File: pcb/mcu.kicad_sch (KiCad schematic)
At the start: 33 parts, among them J1 Conn_01x02_Pin, SW1 SW_SPDT, SW2 SW_Push, SW3 SW_SPDT, U1 TLV1117LV33DCYR, U2 W25Q64JVSSIQ_C179171, U3 STM32H750VBTx, Y1 25 MHz

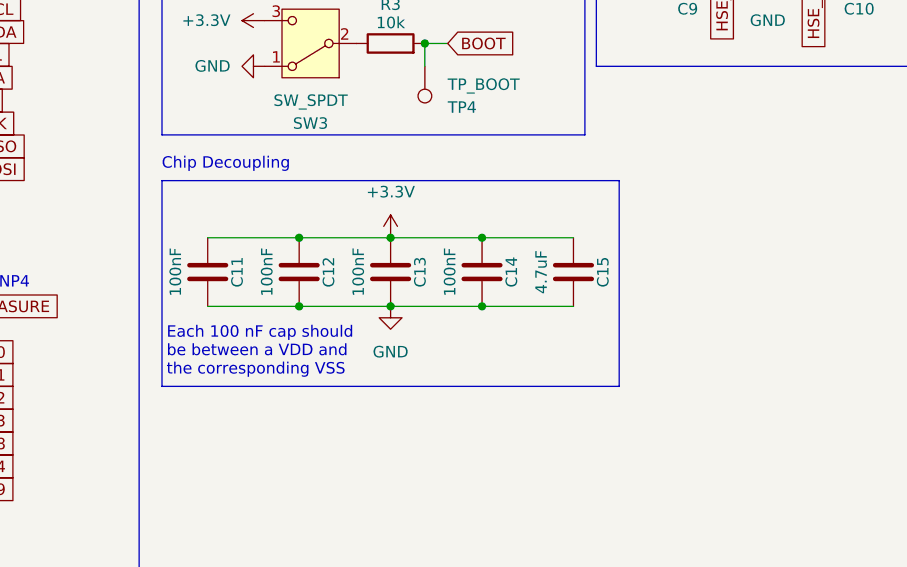
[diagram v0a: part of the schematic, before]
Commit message: [pcb] initial layout and power routing
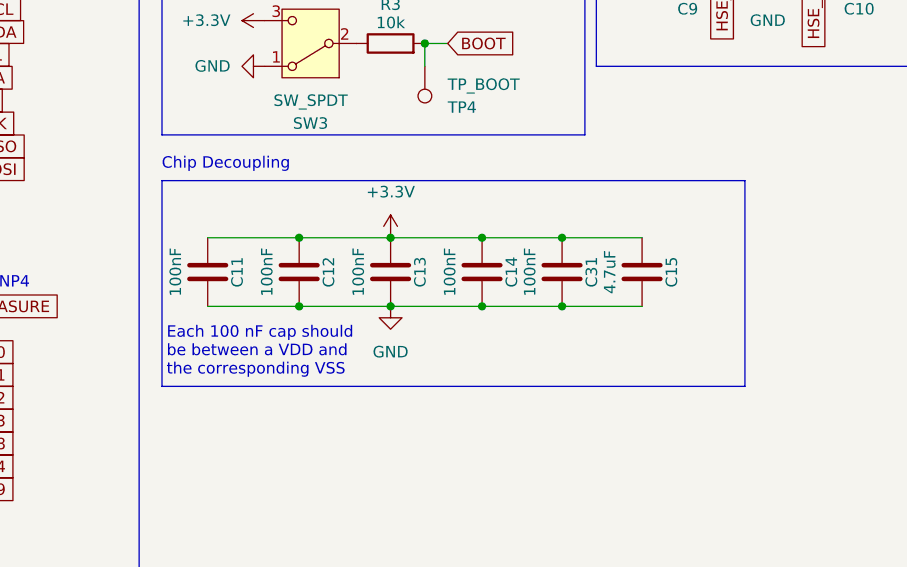
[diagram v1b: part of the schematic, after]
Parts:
- added C31: 100nF, Capacitor_SMD:C_0805_2012Metric_Pad1.18x1.45mm_HandSolder, symbol Device:C
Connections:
- net +3.3V: now also C31.1
- net GND: now also C31.2
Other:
- moved on the sheet: C15
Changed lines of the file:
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@@
 	(rectangle
 		(start 114.3 128.27)
-		(end 165.1 151.13)
+		(end 179.07 151.13)
 		(stroke
 			(width 0)
@@
 	)
 	(junction
+		(at 158.75 134.62)
+		(diameter 0)
+		(color 0 0 0 0)
+	)
+	(junction
 		(at 66.04 180.34)
 		(diameter 0)
@@
 	)
 	(junction
+		(at 158.75 142.24)
+		(diameter 0)
+		(color 0 0 0 0)
+	)
+	(junction
 		(at 62.23 35.56)
 		(diameter 0)
@@
 	(wire
 		(pts
+			(xy 158.75 142.24) (xy 167.64 142.24)
+		)
+		(stroke
+			(width 0)
+			(type default)
+		)
+	)
+	(wire
+		(pts
 			(xy 72.39 30.48) (xy 72.39 35.56)
 		)
@@
 	(wire
 		(pts
+			(xy 158.75 134.62) (xy 167.64 134.62)
+		)
+		(stroke
+			(width 0)
+			(type default)
+		)
+	)
+	(wire
+		(pts
 			(xy 72.39 20.32) (xy 72.39 30.48)
 		)
@@
 	(wire
 		(pts
-			(xy 90.17 39.37) (xy 91.44 39.37)
+			(xy 149.86 134.62) (xy 158.75 134.62)
 		)
 		(stroke
@@
 	(wire
 		(pts
-			(xy 149.86 134.62) (xy 160.02 134.62)
+			(xy 90.17 39.37) (xy 91.44 39.37)
 		)
 		(stroke
@@
 	(wire
 		(pts
-			(xy 149.86 142.24) (xy 160.02 142.24)
+			(xy 149.86 142.24) (xy 158.75 142.24)
 		)
 		(stroke
@@
 	(symbol
 		(lib_id "Device:C")
+		(at 158.75 138.43 0)
+		(unit 1)
+		(exclude_from_sim no)
+		(in_bom yes)
+		(on_board yes)
+		(dnp no)
+		(fields_autoplaced yes)
+		(property "Reference" "C31"
+			(at 162.052 138.43 90)
+			(effects
+				(font
+					(size 1.27 1.27)
+				)
+			)
+		)
+		(property "Value" "100nF"
+			(at 155.194 138.43 90)
+			(effects
+				(font
+					(size 1.27 1.27)
+				)
+			)
+		)
+		(property "Footprint" "Capacitor_SMD:C_0805_2012Metric_Pad1.18x1.45mm_HandSolder"
+			(at 159.7152 142.24 0)
+			(effects
+				(font
+					(size 1.27 1.27)
+				)
+				(hide yes)
+			)
+		)
+		(property "Datasheet" "~"
+			(at 158.75 138.43 0)
+			(effects
+				(font
+					(size 1.27 1.27)
+				)
+				(hide yes)
+			)
+		)
+		(property "Description" "Unpolarized capacitor"
+			(at 158.75 138.43 0)
+			(effects
+				(font
+					(size 1.27 1.27)
+				)
+				(hide yes)
+			)
+		)
+		(pin "1"
+		)
+		(pin "2"
+		)
+		(instances
+			(project "astra"
+				(path "/c0be3de2-9de4-4447-aa6f-537ea5f31aac/0c8c942c-f992-4664-b7a3-b87cb51e1584"
+					(reference "C31")
+					(unit 1)
+				)
+			)
+		)
+	)
+	(symbol
+		(lib_id "Device:C")
 		(at 191.77 101.6 90)
 		(mirror x)
@@
 	(symbol
 		(lib_id "Device:C")
-		(at 160.02 138.43 0)
+		(at 167.64 138.43 0)
 		(unit 1)
 		(exclude_from_sim no)
@@
 		(dnp no)
 		(property "Reference" "C15"
-			(at 163.322 138.43 90)
+			(at 170.942 138.43 90)
 			(effects
 				(font
@@
 		)
 		(property "Value" "4.7uF"
-			(at 156.464 138.43 90)
+			(at 164.084 138.43 90)
 			(effects
 				(font
@@
 		)
 		(property "Footprint" "Capacitor_SMD:C_0805_2012Metric_Pad1.18x1.45mm_HandSolder"
-			(at 160.9852 142.24 0)
+			(at 168.6052 142.24 0)
 			(effects
 				(font
@@
 		)
 		(property "Datasheet" "~"
-			(at 160.02 138.43 0)
+			(at 167.64 138.43 0)
 			(effects
 				(font
@@
 		)
 		(property "Description" "Unpolarized capacitor"
-			(at 160.02 138.43 0)
+			(at 167.64 138.43 0)
 			(effects
 				(font

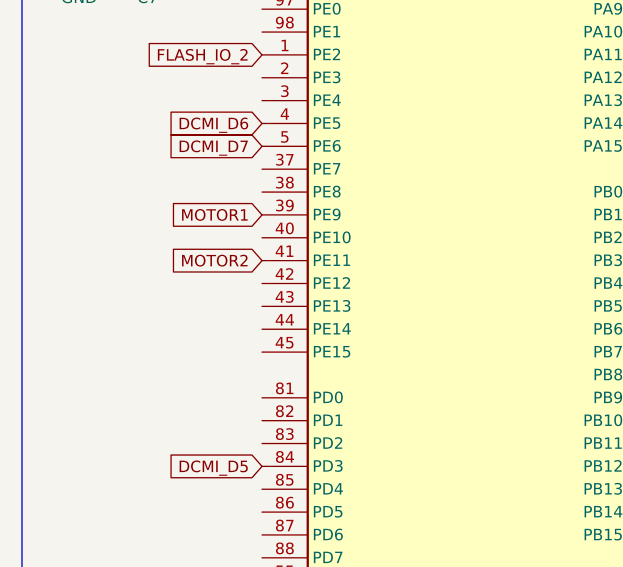
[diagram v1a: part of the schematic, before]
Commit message: [pcb] and [bom] add micro secure digital card interface socket connector
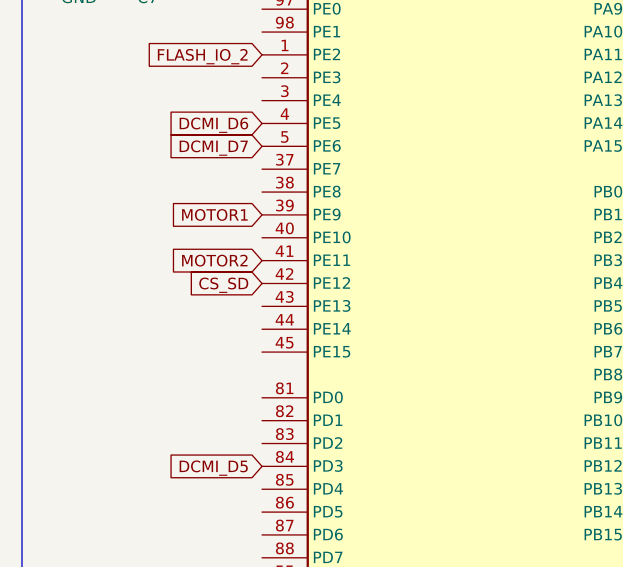
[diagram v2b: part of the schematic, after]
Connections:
- net CS_SD: now reaches U3.42 (PE12)
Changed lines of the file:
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@@
 			(font
 				(size 1.27 1.27)
-				(color 255 255 255 1)
 			)
 		)
@@
 			(font
 				(size 1.27 1.27)
-				(color 255 255 255 1)
 			)
 		)
@@
 			(font
 				(size 1.27 1.27)
-				(color 255 255 255 1)
 			)
 		)
@@
 			(font
 				(size 1.27 1.27)
-				(color 255 255 255 1)
 			)
 			(justify left)
@@
 			(font
 				(size 1.27 1.27)
-				(color 255 255 255 1)
 			)
 		)
@@
 			(effects
 				(font
+					(size 1.27 1.27)
+				)
+				(justify right)
+				(hide yes)
+			)
+		)
+	)
+	(global_label "CS_SD"
+		(shape input)
+		(at 41.91 99.06 180)
+		(fields_autoplaced yes)
+		(effects
+			(font
+				(size 1.27 1.27)
+			)
+			(justify right)
+		)
+		(property "Intersheetrefs" "${INTERSHEET_REFS}"
+			(at 32.9982 99.06 0)
+			(effects
+				(font

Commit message: [pcb] more routing
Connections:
- net DCMI_D0: now also U3.68 (PA9); no longer U3.63 (PC6)
- net DCMI_D2: now also U3.97 (PE0); no longer U3.65 (PC8)
- net DCMI_D3: now also U3.98 (PE1); no longer U3.66 (PC9)
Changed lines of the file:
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@@
+		)
+	)
+	(global_label "DCMI_D0"
+		(shape input)
+		(at 87.63 68.58 0)
+		(fields_autoplaced yes)
+		(effects
+			(font
+				(size 1.27 1.27)
+			)
+			(justify left)
+		)
+		(property "Intersheetrefs" "${INTERSHEET_REFS}"
+			(at 98.6585 68.58 0)
+			(effects
+				(font
+					(size 1.27 1.27)
+				)
+				(justify left)
+				(hide yes)
+			)
 		)
 	)
@@
 		)
 	)
+	(global_label "DCMI_PCLK"
+		(shape input)
+		(at 87.63 60.96 0)
+		(fields_autoplaced yes)
+		(effects
+			(font
+				(size 1.27 1.27)
+			)
+			(justify left)
+		)
+		(property "Intersheetrefs" "${INTERSHEET_REFS}"
+			(at 101.0171 60.96 0)
+			(effects
+				(font
+					(size 1.27 1.27)
+				)
+				(justify left)
+				(hide yes)
+			)
+		)
+	)
+	(global_label "BOOT"
+		(shape input)
+		(at 41.91 50.8 180)
+		(fields_autoplaced yes)
+		(effects
+			(font
+				(size 1.27 1.27)
+			)
+			(justify right)
+		)
+		(property "Intersheetrefs" "${INTERSHEET_REFS}"
+			(at 34.0262 50.8 0)
+			(effects
+				(font
+					(size 1.27 1.27)
+				)
+				(justify right)
+				(hide yes)
+			)
+		)
+	)
 	(global_label "DCMI_D2"
 		(shape input)
-		(at 87.63 152.4 0)
-		(fields_autoplaced yes)
-		(effects
-			(font
-				(size 1.27 1.27)
-			)
-			(justify left)
-		)
-		(property "Intersheetrefs" "${INTERSHEET_REFS}"
-			(at 98.6585 152.4 0)
-			(effects
-				(font
-					(size 1.27 1.27)
-				)
-				(justify left)
-				(hide yes)
-			)
-		)
-	)
-	(global_label "DCMI_PCLK"
-		(shape input)
-		(at 87.63 60.96 0)
-		(fields_autoplaced yes)
-		(effects
-			(font
-				(size 1.27 1.27)
-			)
-			(justify left)
-		)
-		(property "Intersheetrefs" "${INTERSHEET_REFS}"
-			(at 101.0171 60.96 0)
-			(effects
-				(font
-					(size 1.27 1.27)
-				)
-				(justify left)
-				(hide yes)
-			)
-		)
-	)
-	(global_label "BOOT"
-		(shape input)
-		(at 41.91 50.8 180)
-		(fields_autoplaced yes)
-		(effects
-			(font
-				(size 1.27 1.27)
-			)
-			(justify right)
-		)
-		(property "Intersheetrefs" "${INTERSHEET_REFS}"
-			(at 34.0262 50.8 0)
+		(at 41.91 68.58 180)
+		(fields_autoplaced yes)
+		(effects
+			(font
+				(size 1.27 1.27)
+			)
+			(justify right)
+		)
+		(property "Intersheetrefs" "${INTERSHEET_REFS}"
+			(at 30.8815 68.58 0)
 			(effects
 				(font
@@
 		)
 	)
+	(global_label "DCMI_D3"
+		(shape input)
+		(at 41.91 71.12 180)
+		(fields_autoplaced yes)
+		(effects
+			(font
+				(size 1.27 1.27)
+			)
+			(justify right)
+		)
+		(property "Intersheetrefs" "${INTERSHEET_REFS}"
+			(at 30.8815 71.12 0)
+			(effects
+				(font
+					(size 1.27 1.27)
+				)
+				(justify right)
+				(hide yes)
+			)
+		)
+	)
 	(global_label "DCMI_SDA"
 		(shape input)
@@
 		)
 	)
-	(global_label "DCMI_D0"
-		(shape input)
-		(at 87.63 147.32 0)
-		(fields_autoplaced yes)
-		(effects
-			(font
-				(size 1.27 1.27)
-			)
-			(justify left)
-		)
-		(property "Intersheetrefs" "${INTERSHEET_REFS}"
-			(at 98.6585 147.32 0)
-			(effects
-				(font
-					(size 1.27 1.27)
-				)
-				(justify left)
-				(hide yes)
-			)
-		)
-	)
 	(global_label "DCMI_HSYNC"
 		(shape input)
@@
 			(effects
 				(font
-					(size 1.27 1.27)
-				)
-				(justify left)
-				(hide yes)
-			)
-		)
-	)
-	(global_label "DCMI_D3"
-		(shape input)
-		(at 87.63 154.94 0)
-		(fields_autoplaced yes)
-		(effects
-			(font
-				(size 1.27 1.27)
-			)
-			(justify left)
-		)
-		(property "Intersheetrefs" "${INTERSHEET_REFS}"
-			(at 98.6585 154.94 0)
-			(effects
-				(font

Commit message: [pcb] continue routing - motors, camera, battery
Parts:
- removed TP4: TP_BOOT, TestPoint:TestPoint_Pad_D2.0mm, symbol Connector:TestPoint
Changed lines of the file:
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@@
 	)
 	(junction
-		(at 143.51 113.03)
-		(diameter 0)
-		(color 0 0 0 0)
-	)
-	(junction
 		(at 157.48 26.67)
 		(diameter 0)
@@
 	(wire
 		(pts
-			(xy 143.51 113.03) (xy 143.51 115.57)
-		)
-		(stroke
-			(width 0)
-			(type default)
-		)
-	)
-	(wire
-		(pts
 			(xy 209.55 71.12) (xy 208.28 71.12)
 		)
@@
 					(unit 1)
 				)
-			)
-		)
-	)
-	(symbol
-		(lib_id "Connector:TestPoint")
-		(at 143.51 115.57 0)
-		(mirror x)
-		(unit 1)
-		(exclude_from_sim no)
-		(in_bom no)
-		(on_board yes)
-		(dnp no)
-		(property "Reference" "TP4"
-			(at 146.05 120.1421 0)
-			(effects
-				(font
-					(size 1.27 1.27)
-				)
-				(justify left)
-			)
-		)
-		(property "Value" "TP_BOOT"
-			(at 146.05 117.6021 0)
-			(effects
-				(font
-					(size 1.27 1.27)
-				)
-				(justify left)
-			)
-		)
-		(property "Footprint" "TestPoint:TestPoint_Pad_D2.0mm"
-			(at 148.59 115.57 0)
-			(effects
-				(font
-					(size 1.27 1.27)
-				)
-				(hide yes)
-			)
-		)
-		(property "Datasheet" "~"
-			(at 148.59 115.57 0)
-			(effects
-				(font
-					(size 1.27 1.27)
-				)
-				(hide yes)
-			)
-		)
-		(property "Description" "test point"
-			(at 143.51 115.57 0)
-			(effects
-				(font
-					(size 1.27 1.27)
-				)
-				(hide yes)
-			)
-		)
-		(pin "1"
-		)
-		(instances
-			(project "astra"
-				(path "/c0be3de2-9de4-4447-aa6f-537ea5f31aac/0c8c942c-f992-4664-b7a3-b87cb51e1584"
-					(reference "TP4")
-					(unit 1)
-				)

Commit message: [pcb] invented the cutting edge, extremely innovative monke and ddg connectors
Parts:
- removed SW1: SW_SPDT, Button_Switch_THT:SW_Slide-03_Wuerth-WS-SLTV_10x2.5x6.4_P2.54mm, symbol Switch:SW_SPDT
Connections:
- net +BATT: now also J1.1 (Pin_1)
- net DCMI_PWDN: now also U3.87 (PD6); no longer U3.61 (PD14)
- net DCMI_RST: now also U3.88 (PD7); no longer U3.62 (PD15)
- net DDG_MAGIC_1: now reaches U3.18 (PC3_C)
- net DDG_MAGIC_2: now reaches U3.22 (PA0)
- net DDG_MAGIC_3: now reaches U3.23 (PA1)
- net DDG_MAGIC_4: now reaches U3.24 (PA2)
- net DDG_MAGIC_5: now reaches U3.25 (PA3)
- no-connect marks 2 -> 0
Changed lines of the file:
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@@
 	(rectangle
 		(start 179.07 16.51)
-		(end 228.6 35.56)
+		(end 215.9 35.56)
 		(stroke
 			(width 0)
@@
 	(text "ADC1_INP4"
 		(exclude_from_sim no)
-		(at 89.916 139.7 0)
+		(at 104.14 142.494 0)
 		(effects
 			(font
@@
 		(color 0 0 0 0)
 	)
-	(no_connect
-		(at 251.46 -100.33)
-	)
-	(no_connect
-		(at 213.36 25.4)
-	)
 	(wire
 		(pts
@@
 	(wire
 		(pts
-			(xy 200.66 26.67) (xy 200.66 27.94)
-		)
-		(stroke
-			(width 0)
-			(type default)
-		)
-	)
-	(wire
-		(pts
 			(xy 124.46 100.33) (xy 124.46 95.25)
 		)
@@
 	(wire
 		(pts
-			(xy 200.66 27.94) (xy 203.2 27.94)
-		)
-		(stroke
-			(width 0)
-			(type default)
-		)
-	)
-	(wire
-		(pts
 			(xy 66.04 180.34) (xy 64.77 180.34)
 		)
@@
 		)
 	)
+	(global_label "DDG_MAGIC_4"
+		(shape input)
+		(at 87.63 50.8 0)
+		(fields_autoplaced yes)
+		(effects
+			(font
+				(size 1.27 1.27)
+			)
+			(justify left)
+		)
+		(property "Intersheetrefs" "${INTERSHEET_REFS}"
+			(at 103.2547 50.8 0)
+			(effects
+				(font
+					(size 1.27 1.27)
+				)
+				(justify left)
+				(hide yes)
+			)
+		)
+	)
 	(global_label "FLASH_IO_1"
 		(shape input)
@@
 		)
 	)
+	(global_label "DCMI_RST"
+		(shape input)
+		(at 41.91 129.54 180)
+		(fields_autoplaced yes)
+		(effects
+			(font
+				(size 1.27 1.27)
+			)
+			(justify right)
+		)
+		(property "Intersheetrefs" "${INTERSHEET_REFS}"
+			(at 29.9139 129.54 0)
+			(effects
+				(font
+					(size 1.27 1.27)
+				)
+				(justify right)
+				(hide yes)
+			)
+		)
+	)
 	(global_label "TMS"
 		(shape input)
@@
 		)
 	)
+	(global_label "DCMI_PWDN"
+		(shape input)
+		(at 41.91 127 180)
+		(fields_autoplaced yes)
+		(effects
+			(font
+				(size 1.27 1.27)
+			)
+			(justify right)
+		)
+		(property "Intersheetrefs" "${INTERSHEET_REFS}"
+			(at 28.0391 127 0)
+			(effects
+				(font
+					(size 1.27 1.27)
+				)
+				(justify right)
+				(hide yes)
+			)
+		)
+	)
 	(global_label "MOTOR4"
 		(shape input)
@@
 		)
 	)
+	(global_label "DDG_MAGIC_2"
+		(shape input)
+		(at 87.63 45.72 0)
+		(fields_autoplaced yes)
+		(effects
+			(font
+				(size 1.27 1.27)
+			)
+			(justify left)
+		)
+		(property "Intersheetrefs" "${INTERSHEET_REFS}"
+			(at 103.2547 45.72 0)
+			(effects
+				(font
+					(size 1.27 1.27)
+				)
+				(justify left)
+				(hide yes)
+			)
+		)
+	)
 	(global_label "DCMI_PCLK"
 		(shape input)
@@
 		)
 	)
-	(global_label "DCMI_RST"
+	(global_label "DDG_MAGIC_1"
 		(shape input)
-		(at 41.91 149.86 180)
+		(at 87.63 139.7 0)
 		(fields_autoplaced yes)
 		(effects
@@
 				(size 1.27 1.27)
 			)
-			(justify right)
+			(justify left)
 		)
 		(property "Intersheetrefs" "${INTERSHEET_REFS}"
-			(at 29.9139 149.86 0)
+			(at 103.2547 139.7 0)
 			(effects
 				(font
 					(size 1.27 1.27)
 				)
-				(justify right)
+				(justify left)
 				(hide yes)
 			)
@@
 		)
 	)
+	(global_label "DDG_MAGIC_5"
+		(shape input)
+		(at 87.63 53.34 0)
+		(fields_autoplaced yes)
+		(effects
+			(font
+				(size 1.27 1.27)
+			)
+			(justify left)
+		)
+		(property "Intersheetrefs" "${INTERSHEET_REFS}"
+			(at 103.2547 53.34 0)
+			(effects
+				(font
+					(size 1.27 1.27)
+				)
+				(justify left)
+				(hide yes)
+			)
+		)
+	)
 	(global_label "MOTOR3"
 		(shape input)
@@
 		)
 	)
-	(global_label "HSE_I"
+	(global_label "DDG_MAGIC_3"
 		(shape input)
-		(at 41.91 60.96 180)
+		(at 87.63 48.26 0)
 		(fields_autoplaced yes)
 		(effects
@@
 				(size 1.27 1.27)
 			)
-			(justify right)
+			(justify left)
 		)
 		(property "Intersheetrefs" "${INTERSHEET_REFS}"
-			(at 33.6634 60.96 0)
+			(at 103.2547 48.26 0)
 			(effects
 				(font
 					(size 1.27 1.27)
 				)
-				(justify right)
+				(justify left)
 				(hide yes)
 			)
 		)
 	)
-	(global_label "DCMI_HSYNC"
+	(global_label "HSE_I"
 		(shape input)
-		(at 87.63 55.88 0)
+		(at 41.91 60.96 180)
 		(fields_autoplaced yes)
 		(effects
@@
 				(size 1.27 1.27)
 			)
-			(justify left)
+			(justify right)
 		)
 		(property "Intersheetrefs" "${INTERSHEET_REFS}"
-			(at 102.4081 55.88 0)
+			(at 33.6634 60.96 0)
 			(effects
 				(font
 					(size 1.27 1.27)
 				)
-				(justify left)
+				(justify right)
 				(hide yes)
 			)
 		)
 	)
-	(global_label "DCMI_PWDN"
+	(global_label "DCMI_HSYNC"
 		(shape input)
-		(at 41.91 147.32 180)
+		(at 87.63 55.88 0)
 		(fields_autoplaced yes)
 		(effects
@@
 				(size 1.27 1.27)
 			)
-			(justify right)
+			(justify left)
 		)
 		(property "Intersheetrefs" "${INTERSHEET_REFS}"
-			(at 28.0391 147.32 0)
+			(at 102.4081 55.88 0)
 			(effects
 				(font
 					(size 1.27 1.27)
 				)
-				(justify right)
+				(justify left)
 				(hide yes)
 			)
@@
 	(symbol
 		(lib_id "power:+BATT")
-		(at 213.36 30.48 270)
+		(at 200.66 26.67 180)
 		(unit 1)
 		(exclude_from_sim no)
@@
 		(on_board yes)
 		(dnp no)
-		(fields_autoplaced yes)
 		(property "Reference" "#PWR06"
-			(at 209.55 30.48 0)
+			(at 200.66 22.86 0)
 			(effects
 				(font
@@
 		)
 		(property "Value" "+BATT"
-			(at 217.17 30.4799 90)
+			(at 204.724 28.702 0)
 			(effects
 				(font
 					(size 1.27 1.27)
 				)
-				(justify left)
 			)
 		)
 		(property "Footprint" ""
-			(at 213.36 30.48 0)
+			(at 200.66 26.67 0)
 			(effects
 				(font
@@
 		)
 		(property "Datasheet" ""
-			(at 213.36 30.48 0)
+			(at 200.66 26.67 0)
 			(effects
 				(font
@@
 		)
 		(property "Description" "Power symbol creates a global label with name \"+BATT\""
-			(at 213.36 30.48 0)
+			(at 200.66 26.67 0)
 			(effects
 				(font
@@
 		(on_board yes)
 		(dnp no)
-		(fields_autoplaced yes)
 		(property "Reference" "#PWR05"
 			(at 198.12 33.02 0)
@@
 		)
 		(property "Value" "GND"
-			(at 198.12 31.75 0)
+			(at 194.056 28.702 0)
 			(effects
 				(font
@@
 					(unit 1)
 				)
-			)
-		)
-	)
-	(symbol
-		(lib_id "Switch:SW_SPDT")
-		(at 208.28 27.94 0)
-		(unit 1)
-		(exclude_from_sim no)
-		(in_bom yes)
-		(on_board yes)
-		(dnp no)
-		(fields_autoplaced yes)
-		(property "Reference" "SW1"
-			(at 208.28 19.05 0)
-			(effects
-				(font
-					(size 1.27 1.27)
-				)
-			)
-		)
-		(property "Value" "SW_SPDT"
-			(at 208.28 21.59 0)
-			(effects
-				(font
-					(size 1.27 1.27)
-				)
-			)
-		)
-		(property "Footprint" "Button_Switch_THT:SW_Slide-03_Wuerth-WS-SLTV_10x2.5x6.4_P2.54mm"
-			(at 208.28 27.94 0)
-			(effects
-				(font
-					(size 1.27 1.27)
-				)
-				(hide yes)
-			)
-		)
-		(property "Datasheet" "~"
-			(at 208.28 35.56 0)
-			(effects
-				(font
-					(size 1.27 1.27)
-				)
-				(hide yes)
-			)
-		)
-		(property "Description" "Switch, single pole double throw"
-			(at 208.28 27.94 0)
-			(effects
-				(font
-					(size 1.27 1.27)
-				)
-				(hide yes)
-			)
-		)
-		(pin "2"
-		)
-		(pin "3"
-		)
-		(pin "1"
-		)
-		(instances
-			(project ""
-				(path "/c0be3de2-9de4-4447-aa6f-537ea5f31aac/0c8c942c-f992-4664-b7a3-b87cb51e1584"
-					(reference "SW1")
-					(unit 1)
-				)
